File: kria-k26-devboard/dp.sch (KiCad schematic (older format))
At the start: 26 parts, among them J1 47272-0001, U1 74AVC4T245RSVRG4, U2 FIN1019MTC, U3 TPD4E05U06QDQARQ1

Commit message: Routed USB debug part, DP AUX, Supply for SD 3.0, improved decoupling. Other minor improvments
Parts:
- removed D1: PESD2USB5UV-TR, antmicro-footprints:SOT-23s, symbol antmicroTVSDiodes:PESD2USB5UV-TR
- added U55: WE-TVS-824012823, antmicro-footprints:WE_DFN1210-6, symbol antmicroTVSDiodes:WE-TVS-824012823
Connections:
- wire segments 140 -> 144
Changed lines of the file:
@@
 Wire Wire Line
 	4700 3350 4700 3650
-$Comp
-L antmicroTVSDiodes:PESD2USB5UV-TR D1
-U 1 1 647755AA
-P 8100 5700
-F 0 "D1" H 8530 5653 60  0000 L CNN
-F 1 "PESD2USB5UV-TR" H 8530 5547 60  0000 L CNN
-F 2 "antmicro-footprints:SOT-23s" H 8150 5900 60  0001 C CNN
-F 3 "https://assets.nexperia.com/documents/data-sheet/PESD2USB5UV-T.pdf" H 8100 5700 60  0001 C CNN
-F 4 "PESD2USB5UV-TR " H 7800 6000 50  0001 C CNN "MPN"
-F 5 "Nexperia " H 7800 6100 50  0001 C CNN "Manufacturer"
-	1    8100 5700
-	1    0    0    -1
-$EndComp
 Text Label 7950 4750 2    50   ~ 0
 GTR_DP1_M2C_C_P
@@
 Text Label 7950 5050 2    50   ~ 0
 GTR_DP0_M2C_C_N
+Text Label 7800 5800 2    50   ~ 0
+DP_AUX_C_P
 Text Label 7800 5700 2    50   ~ 0
-DP_AUX_C_P
-Text Label 7800 5800 2    50   ~ 0
 DP_AUX_C_N
 Wire Wire Line
@@
 	1    0    0    -1
 $EndComp
+$Comp
+L antmicroTVSDiodes:WE-TVS-824012823 U55
+U 1 1 62C93EF8
+P 8200 5800
+F 0 "U55" H 8200 6125 50  0000 C CNN
+F 1 "WE-TVS-824012823" H 8200 6034 50  0000 C CNN
+F 2 "antmicro-footprints:WE_DFN1210-6" H 8365 5540 50  0001 C CNN
+F 3 "https://www.we-online.com/catalog/datasheet/824012823.pdf" H 8375 5685 50  0001 C CNN
+F 4 "824012823" H 8015 5340 50  0001 C CNN "MPN"
+F 5 "Würth Elektronik" H 8115 5440 50  0001 C CNN "Manufacturer"
+	1    8200 5800
+	1    0    0    -1
+$EndComp
+Text Label 8550 5700 0    50   ~ 0
+DP_AUX_C_N
+Wire Wire Line
+	8550 5700 8500 5700
+Text Label 8550 5800 0    50   ~ 0
+DP_AUX_C_P
+Wire Wire Line
+	8500 5800 8550 5800
+$Comp
+L power:GND #PWR0394
+U 1 1 62CC00F9
+P 8550 5950
+F 0 "#PWR0394" H 8550 5700 50  0001 C CNN
+F 1 "GND" H 8555 5777 50  0000 C CNN
+F 2 "" H 8550 5950 50  0001 C CNN
+F 3 "" H 8550 5950 50  0001 C CNN
+	1    8550 5950
+	1    0    0    -1
+$EndComp
+Wire Wire Line
+	8550 5950 8550 5900
+Wire Wire Line
+	8550 5900 8500 5900
 Wire Bus Line
 	1100 3500 1100 3850

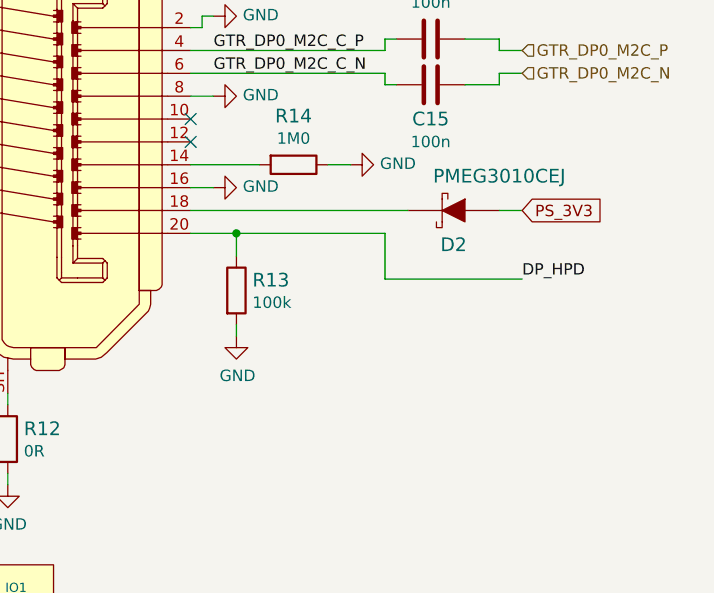
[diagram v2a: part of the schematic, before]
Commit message: Fixed possible FTDI-USB backfeeding issue, finished PS and FTDI power planes creation, finished routing of FTDI/Debug part
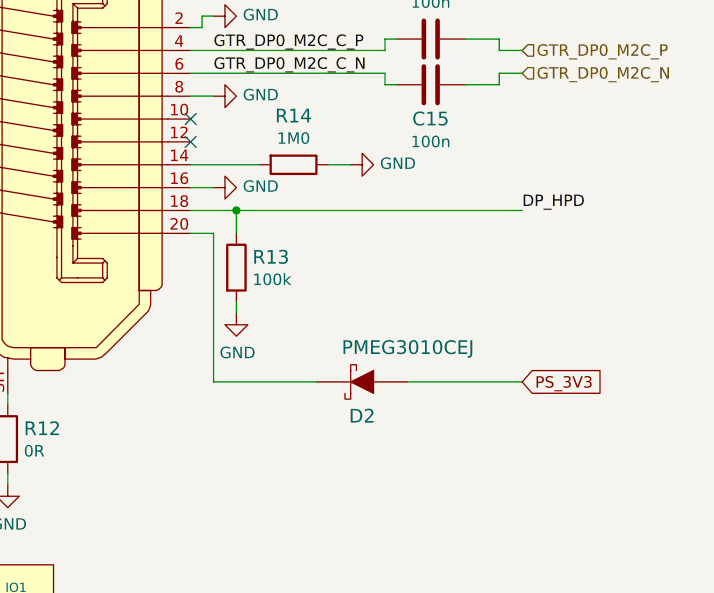
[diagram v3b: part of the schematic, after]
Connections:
- net DP_HPD: now also J1.18; no longer J1.20
- net at D2.K: now also J1.20; no longer J1.18
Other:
- moved on the sheet: D2, R13
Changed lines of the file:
@@
 Wire Wire Line
 	7850 5900 7900 5900
-Text Label 10450 3400 0    50   ~ 0
+Text Label 10450 3100 0    50   ~ 0
 DP_HPD
-Text GLabel 10450 3100 2    50   Input ~ 0
+Text GLabel 10450 3850 2    50   Input ~ 0
 PS_3V3
 $Comp
 L antmicroResistors0402:R_100k_0402 R13
 U 1 1 647C26A3
-P 9200 3450
-F 0 "R13" V 9155 3520 60  0000 L CNN
-F 1 "R_100k_0402" H 9200 3300 60  0001 C CNN
-F 2 "antmicro-footprints:0402-res" H 9400 3650 60  0001 L CNN
-F 3 "" H 9200 3450 50  0001 C CNN
-F 4 "VISHAY" H 9400 3850 60  0001 L CNN "Manufacturer"
-F 5 "CRCW0402100KFKEDHP" H 9400 3750 60  0001 L CNN "MPN"
-F 6 "100k" V 9253 3520 50  0000 L CNN "Val"
-	1    9200 3450
+P 9200 3350
+F 0 "R13" V 9155 3420 60  0000 L CNN
+F 1 "R_100k_0402" H 9200 3200 60  0001 C CNN
+F 2 "antmicro-footprints:0402-res" H 9400 3550 60  0001 L CNN
+F 3 "" H 9200 3350 50  0001 C CNN
+F 4 "VISHAY" H 9400 3750 60  0001 L CNN "Manufacturer"
+F 5 "CRCW0402100KFKEDHP" H 9400 3650 60  0001 L CNN "MPN"
+F 6 "100k" V 9253 3420 50  0000 L CNN "Val"
+	1    9200 3350
 	0    1    1    0
 $EndComp
@@
 L power:GND #PWR024
 U 1 1 647C461A
-P 9200 3650
-F 0 "#PWR024" H 9200 3400 50  0001 C CNN
-F 1 "GND" H 9205 3477 50  0000 C CNN
-F 2 "" H 9200 3650 50  0001 C CNN
-F 3 "" H 9200 3650 50  0001 C CNN
-	1    9200 3650
+P 9200 3550
+F 0 "#PWR024" H 9200 3300 50  0001 C CNN
+F 1 "GND" H 9205 3377 50  0000 C CNN
+F 2 "" H 9200 3550 50  0001 C CNN
+F 3 "" H 9200 3550 50  0001 C CNN
+	1    9200 3550
 	1    0    0    -1
 $EndComp
 Wire Wire Line
-	9200 3650 9200 3600
+	9200 3550 9200 3500
 Wire Wire Line
-	9000 3200 9200 3200
+	9000 3100 9200 3100
 Wire Wire Line
-	9200 3200 9200 3300
+	9200 3100 9200 3200
 $Comp
 L antmicroDiodesRectifiersSingle:PMEG3010CEJ D2
 U 1 1 647D55C5
-P 10150 3100
-F 0 "D2" H 10150 2950 60  0000 C CNN
-F 1 "PMEG3010CEJ" H 9950 3250 60  0000 C CNN
-F 2 "antmicro-footprints:SOD-323F" H 10350 3300 60  0001 L CNN
-F 3 "https://assets.nexperia.com/documents/data-sheet/PMEG3010CEH_PMEG3010CEJ.pdf" H 10350 3400 60  0001 L CNN
-F 4 "PMEG3010CEJ" H 10350 3600 60  0001 L CNN "MPN"
-F 5 "Nexperia" H 10350 4200 60  0001 L CNN "Manufacturer"
-	1    10150 3100
+P 9750 3850
+F 0 "D2" H 9750 3700 60  0000 C CNN
+F 1 "PMEG3010CEJ" H 9550 4000 60  0000 C CNN
+F 2 "antmicro-footprints:SOD-323F" H 9950 4050 60  0001 L CNN
+F 3 "https://assets.nexperia.com/documents/data-sheet/PMEG3010CEH_PMEG3010CEJ.pdf" H 9950 4150 60  0001 L CNN
+F 4 "PMEG3010CEJ" H 9950 4350 60  0001 L CNN "MPN"
+F 5 "Nexperia" H 9950 4950 60  0001 L CNN "Manufacturer"
+	1    9750 3850
 	-1   0    0    -1
 $EndComp
 Wire Wire Line
-	9950 3100 9000 3100
+	9550 3850 9100 3850
 Wire Wire Line
-	10350 3100 10450 3100
-Wire Wire Line
-	9850 3200 9850 3400
-Wire Wire Line
-	9850 3400 10450 3400
-Wire Wire Line
-	9200 3200 9850 3200
-Connection ~ 9200 3200
+	9950 3850 10450 3850
+Connection ~ 9200 3100
 $Comp
 L power:GND #PWR019
@@
 Wire Wire Line
 	8550 5900 8500 5900
+Wire Wire Line
+	9000 3200 9100 3200
+Wire Wire Line
+	9200 3100 10450 3100
+Wire Wire Line
+	9100 3200 9100 3850
 Wire Bus Line
 	1100 3500 1100 3850

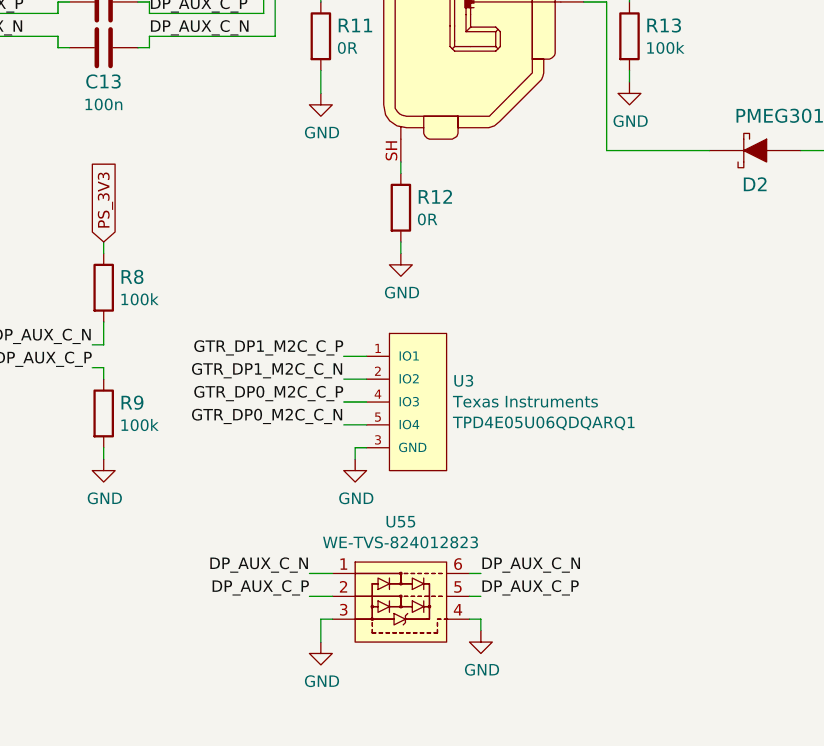
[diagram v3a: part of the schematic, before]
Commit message: Optimization of power planes, fixed missing capacitors on USB 3.0, unify shields, polishing of layout
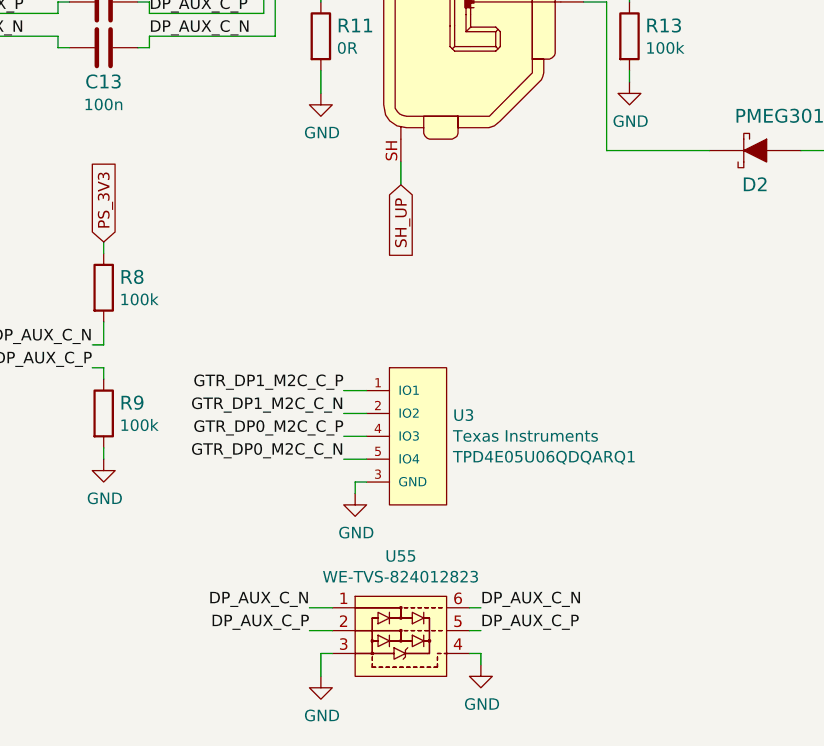
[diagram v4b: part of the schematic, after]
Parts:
- removed R12: R_0R_0402, antmicro-footprints:0402-res, symbol antmicroResistors0402:R_0R_0402
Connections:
- net SH_UP: now reaches J1.SH
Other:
- moved on the sheet: U3, U55
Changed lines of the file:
@@
 L antmicroTVSDiodes:TPD4E05U06QDQARQ1 U3
 U 1 1 63C3CA1D
-P 8100 4950
-F 0 "U3" H 8428 5041 50  0000 L CNN
-F 1 "TPD4E05U06QDQARQ1" H 8150 4550 50  0001 L CNN
-F 2 "antmicro-footprints:TPD4E05U06QDQARQ1" H 8150 5400 50  0001 L CNN
-F 3 "http://www.ti.com/general/docs/lit/getliterature.tsp?genericPartNumber=TPD4E001&fileType=pdf" H 8100 5350 50  0001 L CNN
-F 4 "Texas Instruments" H 8428 4950 50  0000 L CNN "Manufacturer"
-F 5 "TPD4E05U06QDQARQ1" H 8428 4859 50  0000 L CNN "MPN"
-	1    8100 4950
+P 8100 5100
+F 0 "U3" H 8428 5191 50  0000 L CNN
+F 1 "TPD4E05U06QDQARQ1" H 8150 4700 50  0001 L CNN
+F 2 "antmicro-footprints:TPD4E05U06QDQARQ1" H 8150 5550 50  0001 L CNN
+F 3 "http://www.ti.com/general/docs/lit/getliterature.tsp?genericPartNumber=TPD4E001&fileType=pdf" H 8100 5500 50  0001 L CNN
+F 4 "Texas Instruments" H 8428 5100 50  0000 L CNN "Manufacturer"
+F 5 "TPD4E05U06QDQARQ1" H 8428 5009 50  0000 L CNN "MPN"
+	1    8100 5100
 	1    0    0    -1
 $EndComp
@@
 	7850 3100 7850 3200
 $Comp
-L antmicroResistors0402:R_0R_0402 R12
-U 1 1 6458DFAE
-P 8200 4100
-F 0 "R12" V 8155 4170 60  0000 L CNN
-F 1 "R_0R_0402" H 8200 3950 60  0001 C CNN
-F 2 "antmicro-footprints:0402-res" H 8400 4300 60  0001 L CNN
-F 3 "" H 8200 4100 50  0001 C CNN
-F 4 "PANASONIC" H 8400 4500 60  0001 L CNN "Manufacturer"
-F 5 "ERJ2GE0R00X" H 8400 4400 60  0001 L CNN "MPN"
-F 6 "0R" V 8253 4170 50  0000 L CNN "Val"
-	1    8200 4100
-	0    1    1    0
-$EndComp
-$Comp
 L power:GND #PWR023
 U 1 1 6458EAB8
@@
 Wire Wire Line
 	7850 3600 7850 3500
-Wire Wire Line
-	8200 3950 8200 3900
-$Comp
-L power:GND #PWR020
-U 1 1 6459EECB
-P 8200 4300
-F 0 "#PWR020" H 8200 4050 50  0001 C CNN
-F 1 "GND" H 8205 4127 50  0000 C CNN
-F 2 "" H 8200 4300 50  0001 C CNN
-F 3 "" H 8200 4300 50  0001 C CNN
-	1    8200 4300
-	1    0    0    -1
-$EndComp
-Wire Wire Line
-	8200 4300 8200 4250
 Text Label 7100 3250 0    50   ~ 0
 DP_AUX_C_P
@@
 Wire Wire Line
 	4700 3350 4700 3650
-Text Label 7950 4750 2    50   ~ 0
+Text Label 7950 4900 2    50   ~ 0
 GTR_DP1_M2C_C_P
-Text Label 7950 4850 2    50   ~ 0
+Text Label 7950 5000 2    50   ~ 0
 GTR_DP1_M2C_C_N
-Text Label 7950 4950 2    50   ~ 0
+Text Label 7950 5100 2    50   ~ 0
 GTR_DP0_M2C_C_P
-Text Label 7950 5050 2    50   ~ 0
+Text Label 7950 5200 2    50   ~ 0
 GTR_DP0_M2C_C_N
-Text Label 7800 5800 2    50   ~ 0
+Text Label 7800 5950 2    50   ~ 0
 DP_AUX_C_P
-Text Label 7800 5700 2    50   ~ 0
+Text Label 7800 5850 2    50   ~ 0
 DP_AUX_C_N
 Wire Wire Line
-	7800 5800 7900 5800
-Wire Wire Line
-	7800 5700 7900 5700
-Wire Wire Line
-	7950 4750 8050 4750
-Wire Wire Line
-	7950 4850 8050 4850
-Wire Wire Line
-	7950 4950 8050 4950
-Wire Wire Line
-	7950 5050 8050 5050
+	7800 5950 7900 5950
+Wire Wire Line
+	7800 5850 7900 5850
+Wire Wire Line
+	7950 4900 8050 4900
+Wire Wire Line
+	7950 5000 8050 5000
+Wire Wire Line
+	7950 5100 8050 5100
+Wire Wire Line
+	7950 5200 8050 5200
 $Comp
 L power:GND #PWR016
 U 1 1 647A9DF2
-P 7850 6000
-F 0 "#PWR016" H 7850 5750 50  0001 C CNN
-F 1 "GND" H 7855 5827 50  0000 C CNN
-F 2 "" H 7850 6000 50  0001 C CNN
-F 3 "" H 7850 6000 50  0001 C CNN
-	1    7850 6000
-	1    0    0    -1
-$EndComp
-Wire Wire Line
-	7850 6000 7850 5900
-Wire Wire Line
-	7850 5900 7900 5900
+P 7850 6150
+F 0 "#PWR016" H 7850 5900 50  0001 C CNN
+F 1 "GND" H 7855 5977 50  0000 C CNN
+F 2 "" H 7850 6150 50  0001 C CNN
+F 3 "" H 7850 6150 50  0001 C CNN
+	1    7850 6150
+	1    0    0    -1
+$EndComp
+Wire Wire Line
+	7850 6150 7850 6050
+Wire Wire Line
+	7850 6050 7900 6050
 Text Label 10450 3100 0    50   ~ 0
 DP_HPD
@@
 L power:GND #PWR019
 U 1 1 648511DA
-P 8000 5200
-F 0 "#PWR019" H 8000 4950 50  0001 C CNN
-F 1 "GND" H 8005 5027 50  0000 C CNN
-F 2 "" H 8000 5200 50  0001 C CNN
-F 3 "" H 8000 5200 50  0001 C CNN
-	1    8000 5200
-	1    0    0    -1
-$EndComp
-Wire Wire Line
-	8000 5200 8000 5150
-Wire Wire Line
-	8000 5150 8050 5150
+P 8000 5350
+F 0 "#PWR019" H 8000 5100 50  0001 C CNN
+F 1 "GND" H 8005 5177 50  0000 C CNN
+F 2 "" H 8000 5350 50  0001 C CNN
+F 3 "" H 8000 5350 50  0001 C CNN
+	1    8000 5350
+	1    0    0    -1
+$EndComp
+Wire Wire Line
+	8000 5350 8000 5300
+Wire Wire Line
+	8000 5300 8050 5300
 Text Notes 550  750  0    100  ~ 20
 DisplayPort
@@
 L antmicroTVSDiodes:WE-TVS-824012823 U55
 U 1 1 62C93EF8
-P 8200 5800
-F 0 "U55" H 8200 6125 50  0000 C CNN
-F 1 "WE-TVS-824012823" H 8200 6034 50  0000 C CNN
-F 2 "antmicro-footprints:WE_DFN1210-6" H 8365 5540 50  0001 C CNN
-F 3 "https://www.we-online.com/catalog/datasheet/824012823.pdf" H 8375 5685 50  0001 C CNN
-F 4 "824012823" H 8015 5340 50  0001 C CNN "MPN"
-F 5 "Würth Elektronik" H 8115 5440 50  0001 C CNN "Manufacturer"
-	1    8200 5800
-	1    0    0    -1
-$EndComp
-Text Label 8550 5700 0    50   ~ 0
+P 8200 5950
+F 0 "U55" H 8200 6275 50  0000 C CNN
+F 1 "WE-TVS-824012823" H 8200 6184 50  0000 C CNN
+F 2 "antmicro-footprints:WE_DFN1210-6" H 8365 5690 50  0001 C CNN
+F 3 "https://www.we-online.com/catalog/datasheet/824012823.pdf" H 8375 5835 50  0001 C CNN
+F 4 "824012823" H 8015 5490 50  0001 C CNN "MPN"
+F 5 "Würth Elektronik" H 8115 5590 50  0001 C CNN "Manufacturer"
+	1    8200 5950
+	1    0    0    -1
+$EndComp
+Text Label 8550 5850 0    50   ~ 0
 DP_AUX_C_N
 Wire Wire Line
-	8550 5700 8500 5700
-Text Label 8550 5800 0    50   ~ 0
+	8550 5850 8500 5850
+Text Label 8550 5950 0    50   ~ 0
 DP_AUX_C_P
 Wire Wire Line
-	8500 5800 8550 5800
+	8500 5950 8550 5950
 $Comp
 L power:GND #PWR0394
 U 1 1 62CC00F9
-P 8550 5950
-F 0 "#PWR0394" H 8550 5700 50  0001 C CNN
-F 1 "GND" H 8555 5777 50  0000 C CNN
-F 2 "" H 8550 5950 50  0001 C CNN
-F 3 "" H 8550 5950 50  0001 C CNN
-	1    8550 5950
-	1    0    0    -1
-$EndComp
-Wire Wire Line
-	8550 5950 8550 5900
-Wire Wire Line
-	8550 5900 8500 5900
+P 8550 6100
+F 0 "#PWR0394" H 8550 5850 50  0001 C CNN
+F 1 "GND" H 8555 5927 50  0000 C CNN
+F 2 "" H 8550 6100 50  0001 C CNN
+F 3 "" H 8550 6100 50  0001 C CNN
+	1    8550 6100
+	1    0    0    -1
+$EndComp
+Wire Wire Line
+	8550 6100 8550 6050
+Wire Wire Line
+	8550 6050 8500 6050
 Wire Wire Line
 	9000 3200 9100 3200
@@
 Wire Wire Line
 	9100 3200 9100 3850
+Wire Wire Line
+	8200 3900 8200 4000
 Wire Bus Line
 	1100 3500 1100 3850
+Text GLabel 8200 4000 3    50   Input ~ 0
+SH_UP
 $EndSCHEMATC

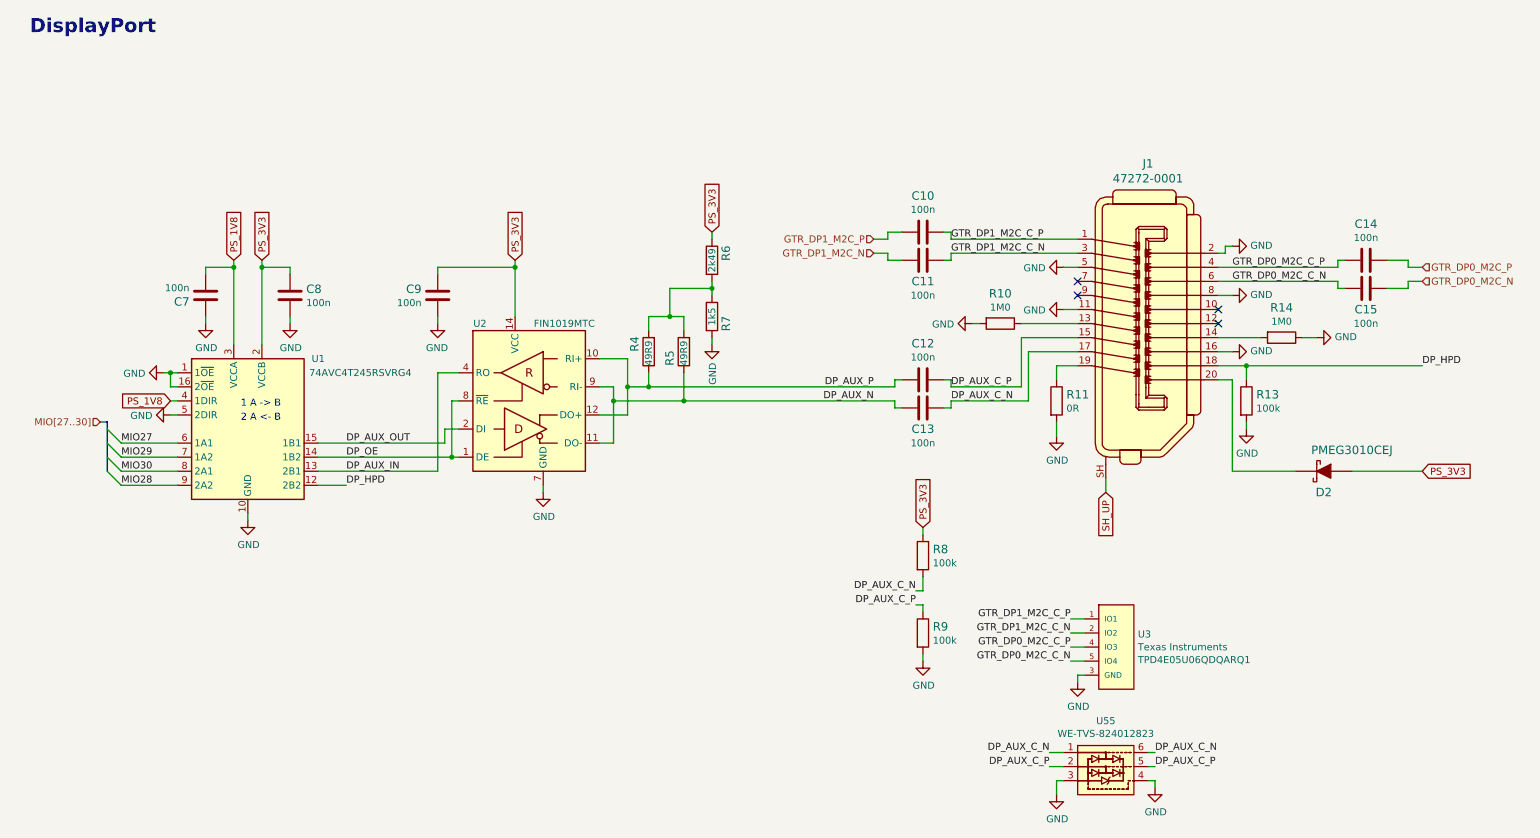
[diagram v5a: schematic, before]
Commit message: Fixed missing USB - M2 connection, finishing touches of PCB
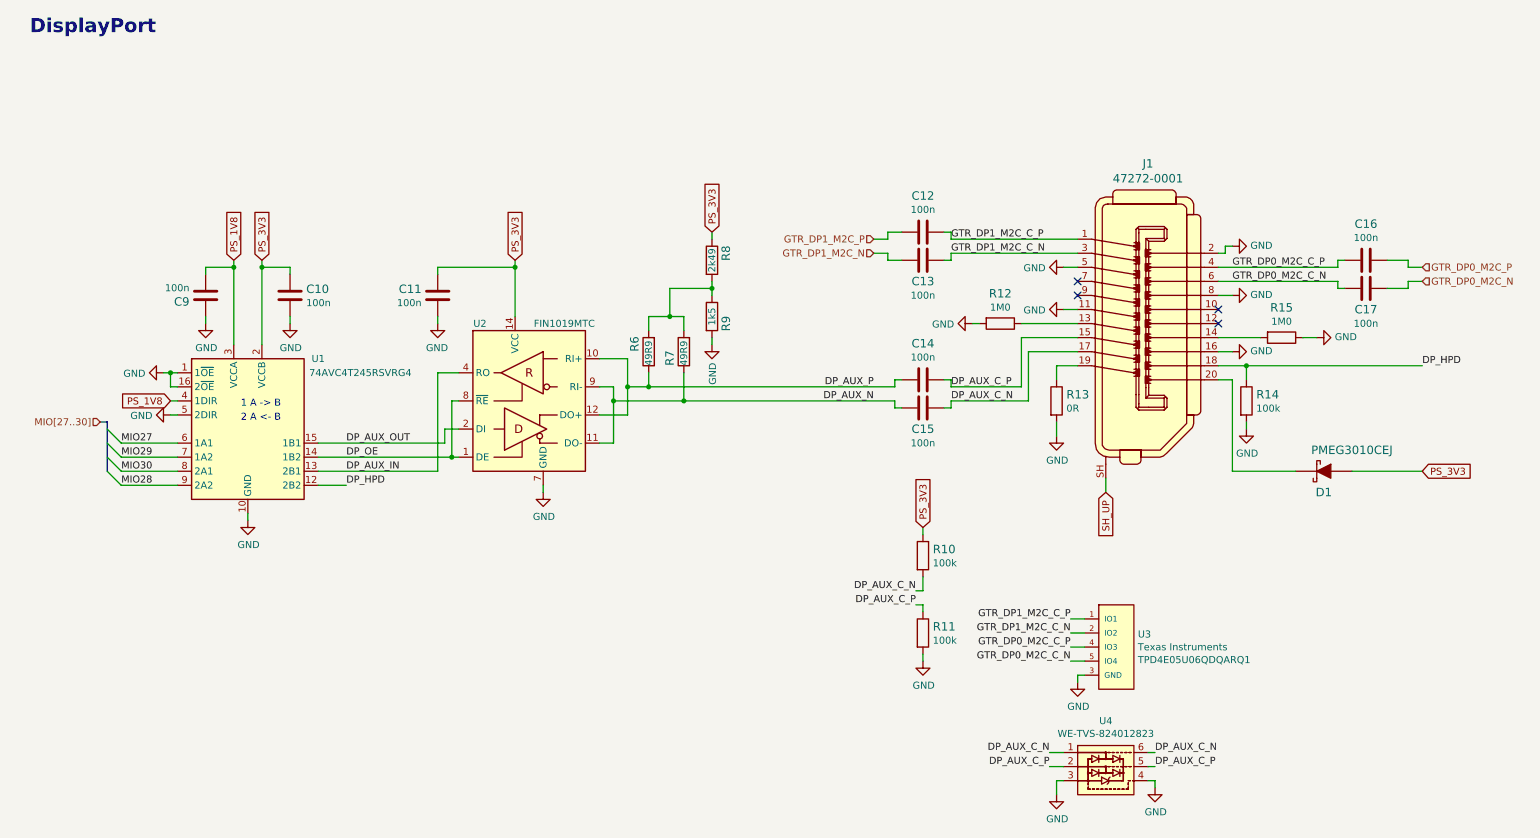
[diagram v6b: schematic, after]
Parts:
- renumbered C8 to C10, C9 to C11, C10 to C12, C11 to C13, C12 to C14, C13 to C15, C14 to C16, C15 to C17, C7 to C9, D2 to D1, R8 to R10, R9 to R11, R10 to R12, R11 to R13, R13 to R14, R14 to R15, R4 to R6, R5 to R7, R6 to R8, R7 to R9, U55 to U4
